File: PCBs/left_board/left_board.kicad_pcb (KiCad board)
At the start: 2 copper layers, 143.8 x 139.6 mm, 98 parts, among them J101 USB4510-03-1-A, J102 Conn_ARM_SWD_TagConnect_TC2030, J103 GSB12J21C1EU, J104 USB4510-03-1-A, SW101 SW_DIP_x01, SW102 SW_DIP_x01, SW103 SW_DIP_x01, SW104 SW_DIP_x01, SW105 SW_DIP_x01, SW106 SW_DIP_x01, SW107 SW_DIP_x01, SW108 SW_DIP_x01, SW109 SW_DIP_x01, SW110 SW_DIP_x01, SW111 SW_DIP_x01, SW112 SW_DIP_x01, SW113 SW_DIP_x01, SW114 SW_DIP_x01, SW115 SW_DIP_x01, SW116 SW_DIP_x01, SW117 SW_DIP_x01, SW118 SW_DIP_x01, SW119 SW_DIP_x01, SW120 SW_DIP_x01, SW121 SW_DIP_x01, SW122 SW_DIP_x01, SW123 SW_DIP_x01, SW124 SW_DIP_x01, SW125 SW_DIP_x01, SW126 SW_DIP_x01, SW127 SW_DIP_x01, SW128 RIC11-31S15.5D7-TH, U101 STM32G0C1CEUx, U102 USB2533-1080AEN, U103 M24256X-FCU6T_VF, U104 USBLC6-4SC6, U105 USBLC6-4SC6, U106 USBLC6-4SC6, Y101 CX2016SA24000D0HLLG3

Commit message: Left board routing half done
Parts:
- C109, C110, C111: moved to B.Cu
- moved D101 110.8 mm to (201.9, 142.0), turned to 150 degrees
- moved D118 109.1 mm to (141.3, 51.3), turned to 180 degrees
- moved D109 107.5 mm to (84.3, 97.3), turned to 180 degrees
- moved SW124 107.5 mm to (200.1, 146.4), turned to -30 degrees
- moved SW121 101.4 mm to (180.0, 47.0), turned to 0 degrees
- moved SW116 96.0 mm to (184.9, 134.8), turned to -30 degrees
- moved SW122 95.0 mm to (180.0, 66.0)
- moved SW123 95.0 mm to (180.0, 85.0)
- moved SW114 89.7 mm to (142.0, 56.0), turned to 0 degrees
- moved D102 88.4 mm to (186.6, 130.4), turned to 150 degrees
- moved D125 86.5 mm to (141.3, 32.3), turned to 0 degrees
- moved SW104 86.5 mm to (85.0, 102.0)
- moved SW118 85.4 mm to (161.0, 63.0)
- moved D126 81.3 mm to (160.3, 39.3), turned to 0 degrees
- moved SW107 77.0 mm to (104.0, 83.0), turned to 0 degrees
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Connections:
- R101 pad 1: +3V3 -> +3.3V
- R102 pad 1: +3V3 -> +3.3V
- SW106 pad 2: /KEY_B3 -> /KEY_B2
- SW107 pad 2: /KEY_C3 -> /KEY_C2
- SW108 pad 2: /KEY_D3 -> /KEY_D2
- SW116 pad 2: /KEY_D4 -> /KEY_E2
- SW120 pad 2: /KEY_D5 -> /KEY_D6
- SW124 pad 2: /KEY_D6 -> /KEY_E3
- SW126 pad 2: /KEY_E2 -> /KEY_D4
- SW127 pad 2: /KEY_E3 -> /KEY_D5
- U101 pad 1: unconnected-(U101-PC13-Pad1) -> /KEY_E1
- U101 pad 11: unconnected-(U101-PA0-Pad11) -> /KEY_D3
- U101 pad 12: unconnected-(U101-PA1-Pad12) -> /KEY_D4
- U101 pad 13: unconnected-(U101-PA2-Pad13) -> /KEY_D5
- U101 pad 25: unconnected-(U101-PB13-Pad25) -> /SCL
- U101 pad 26: unconnected-(U101-PB14-Pad26) -> /SDA
- U101 pad 4: +3V3 -> +3.3V
- U101 pad 43: unconnected-(U101-PB4-Pad43) -> /ENC_A
- U101 pad 44: unconnected-(U101-PB5-Pad44) -> /ENC_B
- U101 pad 45: unconnected-(U101-PB6-Pad45) -> /ENC_SW
- U101 pad 46: unconnected-(U101-PB7-Pad46) -> /LED1
- U101 pad 47: unconnected-(U101-PB8-Pad47) -> /KEY_E3
- U101 pad 48: unconnected-(U101-PB9-Pad48) -> /KEY_E2
- U101 pad 6: +3V3 -> +3.3V
- U101 pad 8: unconnected-(U101-PF0-Pad8) -> /KEY_D1
- U101 pad 9: unconnected-(U101-PF1-Pad9) -> /KEY_D2
- U102 pad 10: +3V3 -> +3.3V
- U102 pad 15: +3V3 -> +3.3V
- U102 pad 23: +3V3 -> +3.3V
- U102 pad 26: +3V3 -> +3.3V
- U102 pad 29: +3V3 -> +3.3V
- U102 pad 36: +3V3 -> +3.3V
- U103 pad A1: +3V3 -> +3.3V
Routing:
- net /USB0_CC2: track 9.00 -> 186.4 mm, vias 1 -> 2
- net /USB0_CC1: track 8.74 -> 186.1 mm, vias 1 -> 2
- net /USB2_DP: track 0.00 -> 155.7 mm, vias 0 -> 2
- net /KEY_A1: track 0.00 -> 155.4 mm
- net /USB2_DN: track 0.00 -> 154.7 mm
- net /KEY_A2: track 0.00 -> 131.0 mm
- net /USB1_CC1: track 0.00 -> 120.5 mm, vias 0 -> 3
- net GND: track 0.00 -> 119.9 mm, vias 9 -> 80
- net /USB1_CC2: track 0.00 -> 119.2 mm, vias 0 -> 3
- net /KEY_A3: track 0.00 -> 108.6 mm
- net /KEY_D1: track 0.00 -> 102.9 mm
- net /SCL: track 3.20 -> 105.1 mm
- net /SDA: track 2.11 -> 102.0 mm
- net /KEY_A4: track 0.00 -> 82.0 mm
- net /KEY_D2: track 0.00 -> 80.4 mm
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- added copper zone on F.Cu, net GND

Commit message: Left board done
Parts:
- added C105: 1u, Capacitor_SMD:C_0402_1005Metric, B.Cu at (116.9, 35.7)
- added C106: 100n, Capacitor_SMD:C_0402_1005Metric, B.Cu at (105.9, 36.9)
- added D128: WHITE, LED_SMD:LED_0402_1005Metric, B.Cu at (196.1, 105.9)
- added D129: WHITE, LED_SMD:LED_0402_1005Metric, B.Cu at (197.5, 105.9)
- added R106: 3k3, Resistor_SMD:R_0402_1005Metric, F.Cu at (196.5, 99.3)
- added R107: 3k3, Resistor_SMD:R_0402_1005Metric, F.Cu at (202.8, 102.9)
- R101, R102: moved to B.Cu
- moved U103 99.3 mm to (128.7, 41.6)
- moved R102 97.5 mm to (128.7, 39.9), turned to 180 degrees
- moved R101 94.0 mm to (130.3, 41.6), turned to -90 degrees
- moved REF** 2.67 mm to (207.3, 107.2)
- moved J102 1.51 mm to (208.3, 134.1), turned to 180 degrees
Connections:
- U101 pad 11: /KEY_D3 -> /KEY_C1
- U101 pad 12: /KEY_D4 -> /KEY_C2
- U101 pad 13: /KEY_D5 -> /KEY_C3
- U101 pad 14: unconnected-(U101-PA3-Pad14) -> /KEY_C4
- U101 pad 15: unconnected-(U101-PA4-Pad15) -> /KEY_D5
- U101 pad 16: unconnected-(U101-PA5-Pad16) -> /KEY_B1
- U101 pad 17: unconnected-(U101-PA6-Pad17) -> /KEY_B2
- U101 pad 18: unconnected-(U101-PA7-Pad18) -> /KEY_B3
- U101 pad 19: unconnected-(U101-PB0-Pad19) -> /KEY_B4
- U101 pad 2: unconnected-(U101-PC14-Pad2) -> /KEY_D1
- U101 pad 20: unconnected-(U101-PB1-Pad20) -> /KEY_A1
- U101 pad 21: unconnected-(U101-PB2-Pad21) -> /KEY_C5
- U101 pad 22: unconnected-(U101-PB10-Pad22) -> /KEY_A2
- U101 pad 23: unconnected-(U101-PB11-Pad23) -> /KEY_B5
- U101 pad 24: unconnected-(U101-PB12-Pad24) -> /KEY_A3
- U101 pad 29: unconnected-(U101-PA9/UCPD1_DBCC1-Pad29) -> /KEY_D6
- U101 pad 3: unconnected-(U101-PC15-Pad3) -> /KEY_D2
- U101 pad 30: unconnected-(U101-PC6-Pad30) -> /KEY_A4
- U101 pad 31: unconnected-(U101-PC7-Pad31) -> /KEY_A5
- U101 pad 32: unconnected-(U101-PA10/UCPD1_DBCC2-Pad32) -> /KEY_A6
- U101 pad 37: unconnected-(U101-PA15-Pad37) -> /KEY_B6
- U101 pad 39: unconnected-(U101-PD1-Pad39) -> /KEY_C6
- U101 pad 41: unconnected-(U101-PD3-Pad41) -> /STAT1
- U101 pad 42: unconnected-(U101-PB3-Pad42) -> /STAT2
- U101 pad 8: /KEY_D1 -> /KEY_D3
- U101 pad 9: /KEY_D2 -> /KEY_D4
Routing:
- net +3.3V: track 15.9 -> 333.1 mm, vias 8 -> 46
- net VBUS: track 7.20 -> 115.9 mm, vias 3 -> 57
- net /USB0_CC2: track 186.4 -> 283.0 mm, vias 2 -> 3
- net /USB0_CC1: track 186.1 -> 281.1 mm, vias 2 -> 3
- net /KEY_B1: track 76.5 -> 139.2 mm
- net /KEY_C1: track 69.9 -> 132.3 mm
- net /KEY_C2: track 48.8 -> 109.4 mm
- net /SDA: track 102.0 -> 160.9 mm, vias 1 -> 2
- net /KEY_C3: track 29.3 -> 88.2 mm
- net /KEY_B5: track 0.00 -> 57.5 mm
- net /KEY_C4: track 16.0 -> 73.1 mm
- net /SCL: track 105.1 -> 160.5 mm, vias 1 -> 2
- net /KEY_B2: track 64.6 -> 114.3 mm
- net /SWDIO: track 0.00 -> 49.5 mm, vias 0 -> 2
- net GND: track 119.9 -> 169.0 mm, vias 80 -> 95
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- added copper zone on B.Cu, net +3.3V
- added copper zone on B.Cu, net VBUS

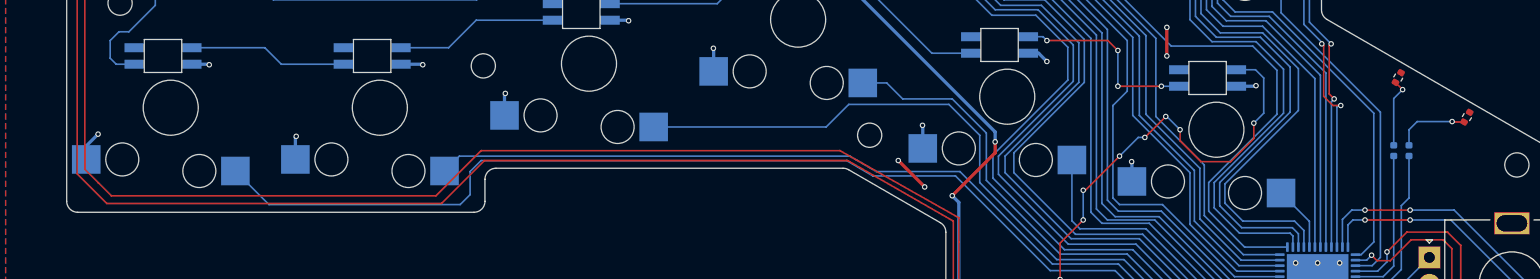
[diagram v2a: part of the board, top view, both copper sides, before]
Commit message: Right board done, all components ordered
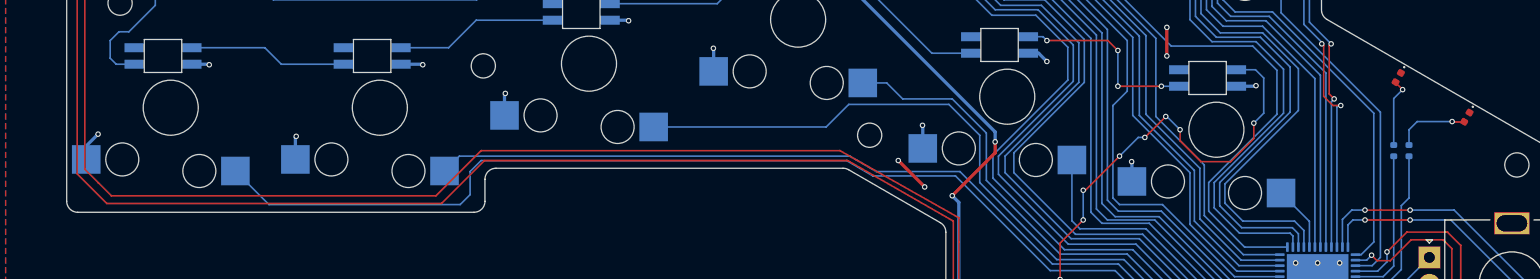
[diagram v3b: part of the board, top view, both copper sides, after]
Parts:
- D128, D129: moved to F.Cu
- R106, R107: moved to B.Cu
- moved D128 6.65 mm to (196.5, 99.3), turned to -120 degrees
- moved R106 6.65 mm to (196.1, 105.9), turned to 90 degrees
- moved D129 6.07 mm to (202.8, 102.9), turned to -120 degrees
- moved R107 6.07 mm to (197.5, 105.9), turned to -90 degrees
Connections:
- D128 pad 1: /STAT1_K -> GND
- D128 pad 2: /STAT1 -> /STAT1_K
- D129 pad 1: /STAT2_K -> GND
- D129 pad 2: /STAT2 -> /STAT2_K
- R106 pad 1: /STAT1_K -> /STAT1
- R106 pad 2: GND -> /STAT1_K
- R107 pad 2: GND -> /STAT2
